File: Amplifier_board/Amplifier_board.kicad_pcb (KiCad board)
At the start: 2 copper layers, 100 x 100 mm, 167 parts, among them J1 Screw Terminal, J10 Conn_01x03_Pin, J11 Conn_01x03_Pin, J12 Conn_01x03_Pin, J13 Conn_01x03_Pin, J14 Conn_01x03_Pin, J15 Conn_01x03_Pin, J2 Screw Terminal, J3 Screw Terminal, J4 Screw Terminal, J5 Screw Terminal, J6 Screw Terminal, J7 A-DF_09_A_KG-T4S, J8 Conn_01x03_Pin, J9 Conn_01x03_Pin, U1 TPA3111D1PWPR, U2 TPA3111D1PWPR, U3 TPA3111D1PWPR, U4 TPA3111D1PWPR

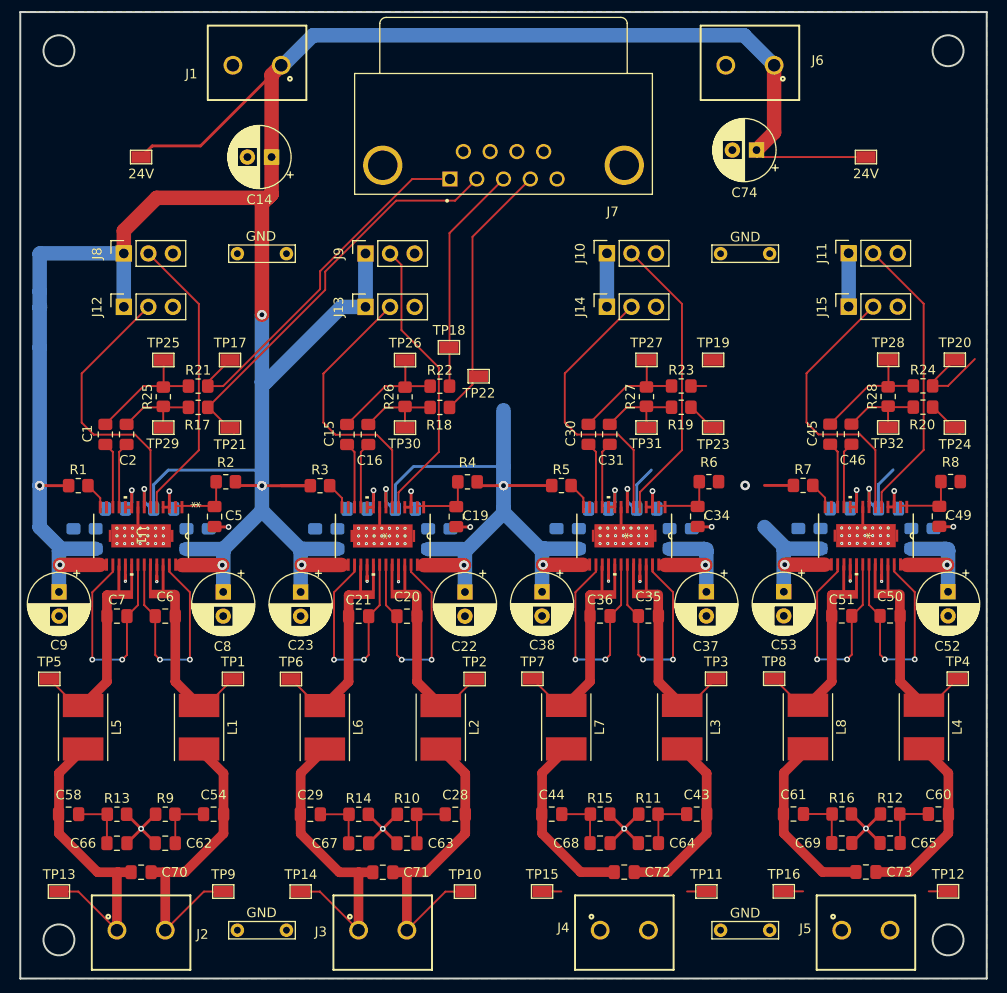
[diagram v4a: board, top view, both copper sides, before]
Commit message: Added test points, almost finished layout for amp board
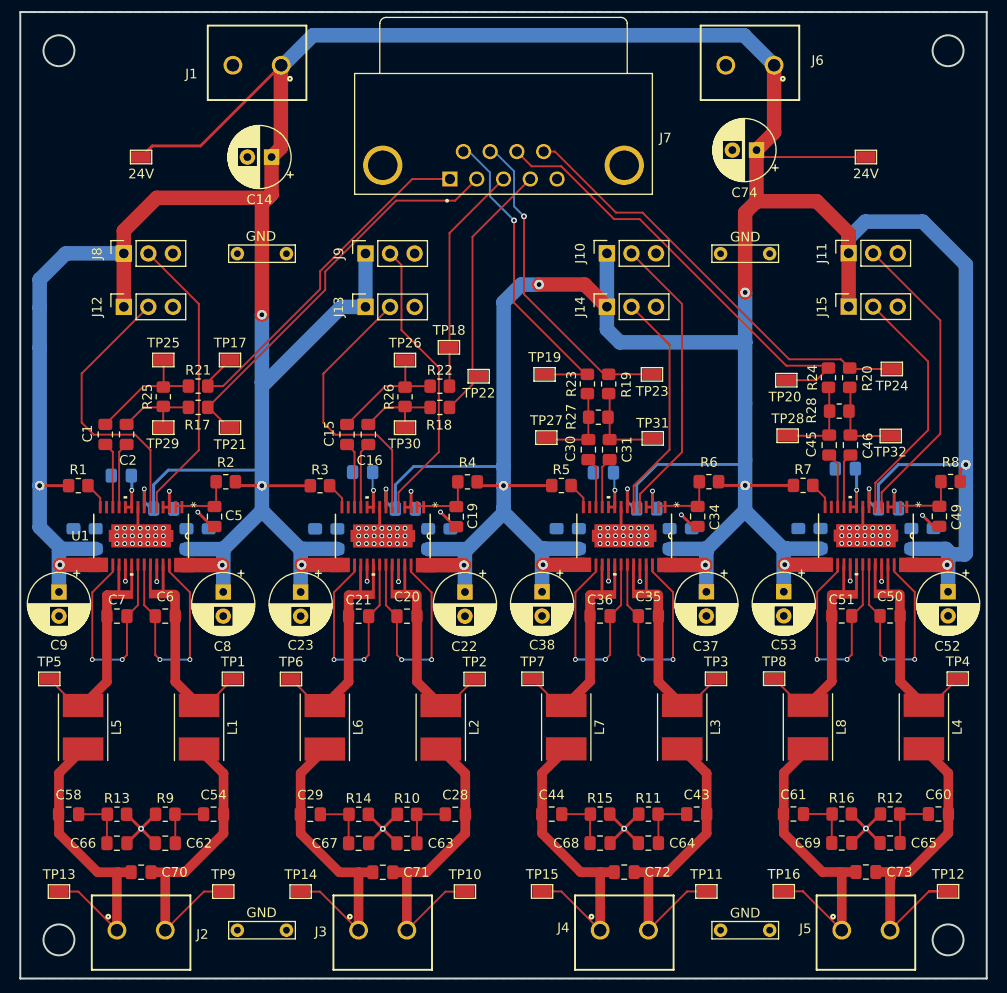
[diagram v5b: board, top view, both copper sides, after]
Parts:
- moved TP20 17.6 mm to (153.8, 77.6)
- moved TP19 17.5 mm to (128.8, 77.0)
- moved TP27 13.1 mm to (128.9, 83.5)
- moved TP28 13.0 mm to (153.9, 83.3)
- moved R24 9.82 mm to (158.1, 77.3), turned to 90 degrees
- moved R23 9.71 mm to (133.2, 78.0), turned to 90 degrees
- moved TP24 8.89 mm to (164.7, 76.4)
- moved TP23 8.39 mm to (139.9, 77.0)
- moved R20 8.17 mm to (160.3, 77.3), turned to 90 degrees
- moved R19 7.89 mm to (135.4, 78.0), turned to 90 degrees
- moved R27 5.42 mm to (134.3, 81.4), turned to 180 degrees
- moved R28 5.28 mm to (159.2, 80.8), turned to 180 degrees
- moved C48 4.17 mm to (159.9, 86.7)
- moved C18 3.84 mm to (109.9, 87.1)
- moved C33 3.77 mm to (134.8, 87.2)
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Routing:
- net +24V: track 455.1 -> 622.9 mm, vias 17 -> 20
- net /In4N: track 3.87 -> 45.3 mm
- net /In4P: track 9.74 -> 46.4 mm
- net /In3P: track 2.56 -> 33.8 mm, vias 0 -> 1
- net /In3N: track 3.87 -> 33.2 mm, vias 0 -> 1
- net /amp4/OutN: track 20.9 -> 34.7 mm
- net /amp4/OutP: track 20.9 -> 32.7 mm
- net /amp3/OutP: track 20.9 -> 32.6 mm
- net /amp3/OutN: track 20.9 -> 32.6 mm
- net /amp3/Gain1: track 29.0 -> 23.9 mm
- net Net-(C30-Pad1): track 13.2 -> 9.23 mm
- net Net-(C45-Pad1): track 13.2 -> 9.30 mm
- net /amp4/Gain1: track 29.0 -> 25.3 mm
- net Net-(U3-INN): track 6.81 -> 5.23 mm
- net Net-(U3-INP): track 6.81 -> 5.23 mm
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
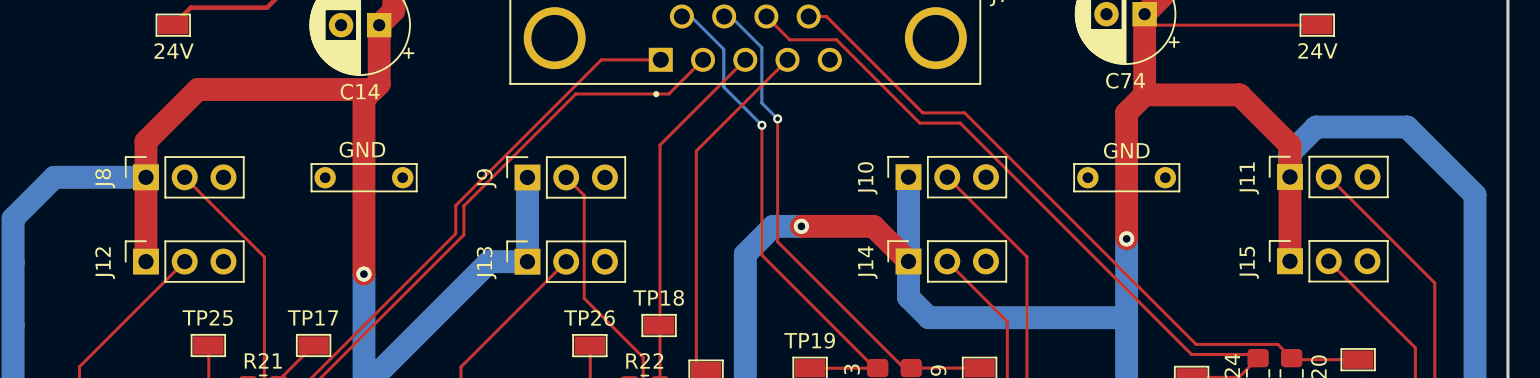
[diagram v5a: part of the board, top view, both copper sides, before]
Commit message: Updated silkscreen on amp board
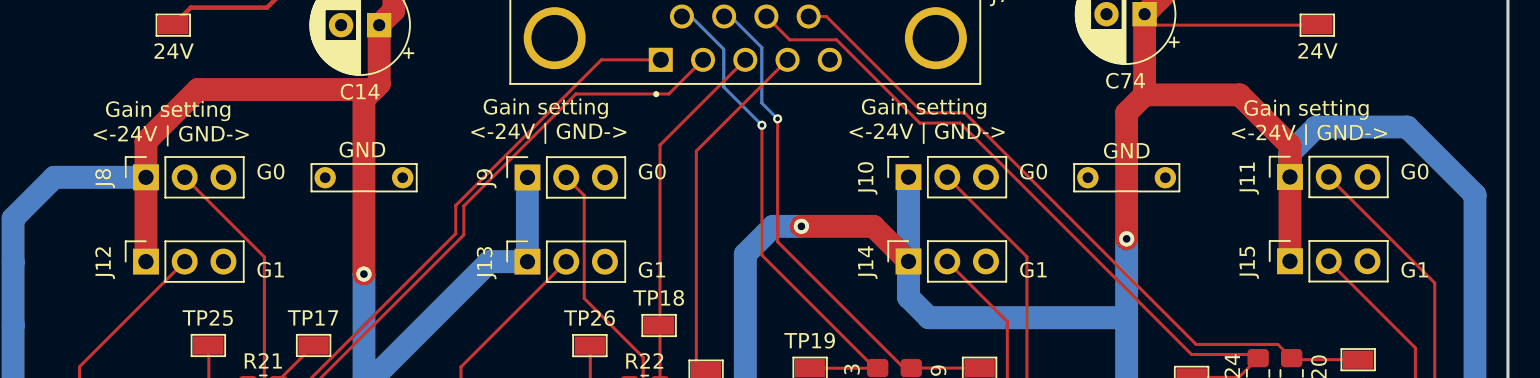
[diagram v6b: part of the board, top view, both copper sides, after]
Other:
- board text added: "G0 G1"
- board text added: "Gain setting <-24V | GND->"

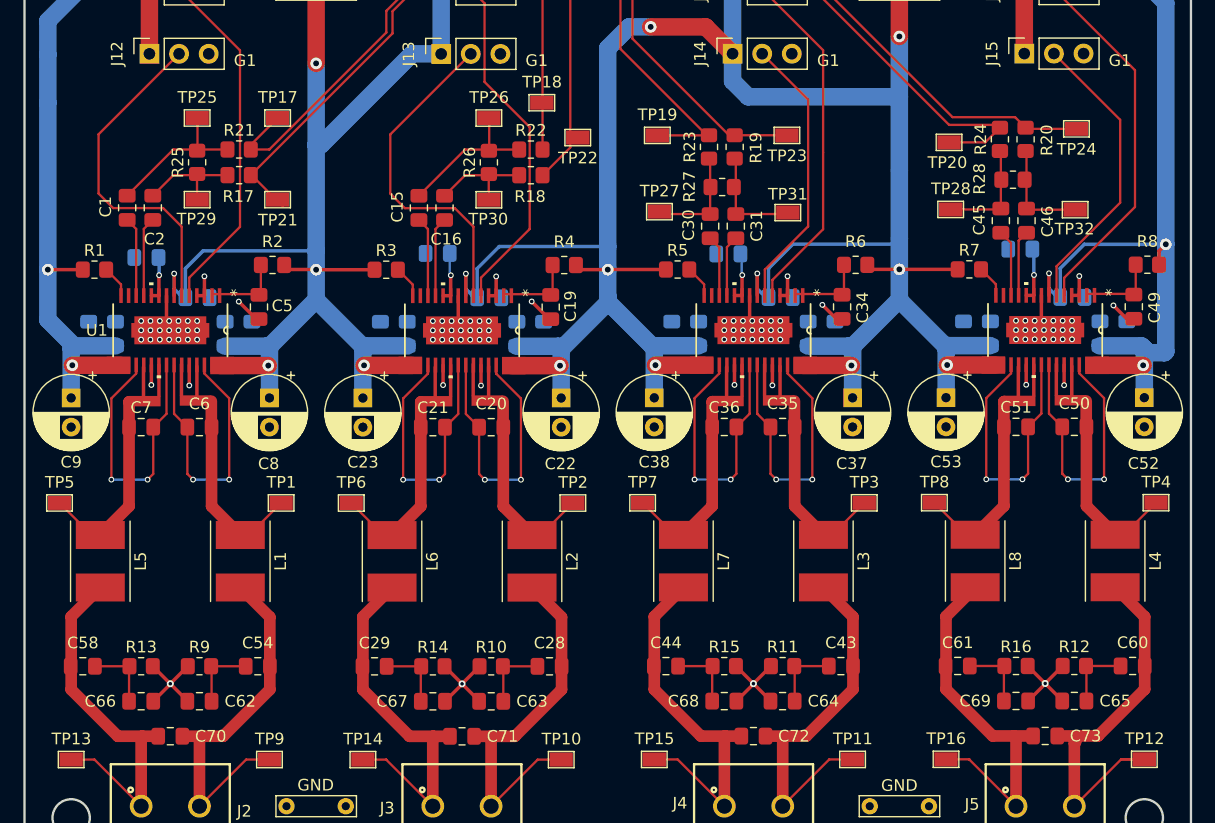
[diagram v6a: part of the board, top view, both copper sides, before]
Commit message: Added new MCU board footprint and symbol
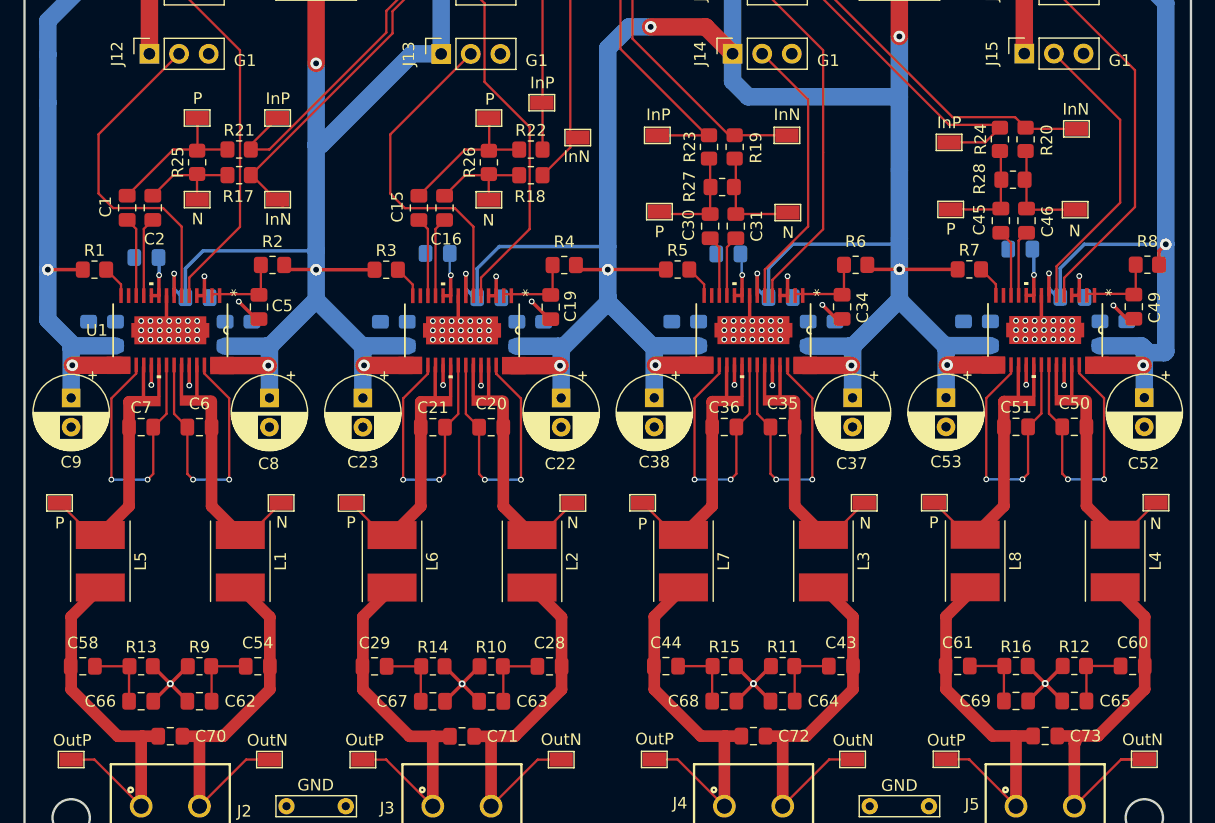
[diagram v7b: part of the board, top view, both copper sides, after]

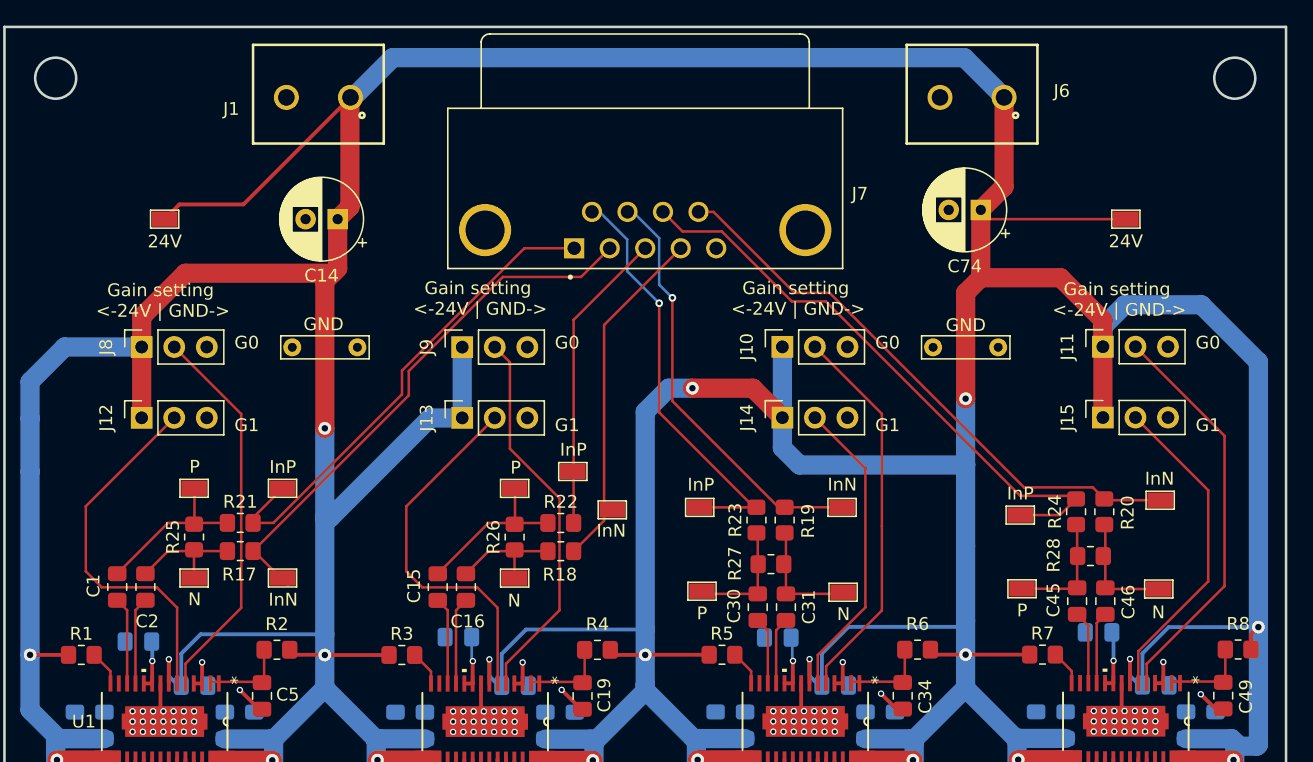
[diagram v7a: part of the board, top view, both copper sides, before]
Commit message: Schematic almost done on DAC board
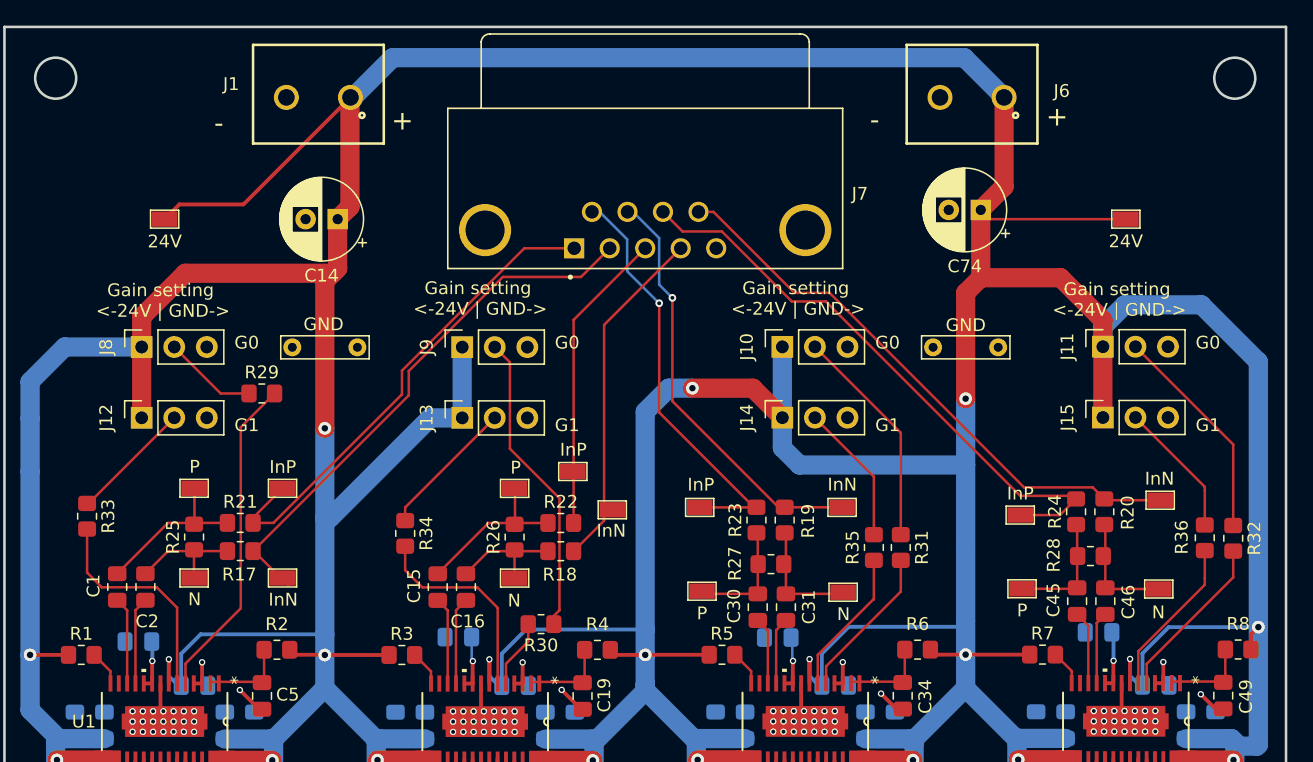
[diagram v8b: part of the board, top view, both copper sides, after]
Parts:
- added R29: 100k, Resistor_SMD:R_0805_2012Metric_Pad1.20x1.40mm_HandSolder, F.Cu at (94.6, 68.1)
- added R30: 100k, Resistor_SMD:R_0805_2012Metric_Pad1.20x1.40mm_HandSolder, F.Cu at (116.4, 86.1)
- added R31: 100k, Resistor_SMD:R_0805_2012Metric_Pad1.20x1.40mm_HandSolder, F.Cu at (144.4, 80.1)
- added R32: 100k, Resistor_SMD:R_0805_2012Metric_Pad1.20x1.40mm_HandSolder, F.Cu at (170.4, 79.4)
- added R33: 100k, Resistor_SMD:R_0805_2012Metric_Pad1.20x1.40mm_HandSolder, F.Cu at (81.0, 77.7)
- added R34: 100k, Resistor_SMD:R_0805_2012Metric_Pad1.20x1.40mm_HandSolder, F.Cu at (105.8, 79.0)
- added R35: 100k, Resistor_SMD:R_0805_2012Metric_Pad1.20x1.40mm_HandSolder, F.Cu at (142.3, 80.1)
- added R36: 100k, Resistor_SMD:R_0805_2012Metric_Pad1.20x1.40mm_HandSolder, F.Cu at (168.2, 79.4)
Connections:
- J10 pad 2: /amp3/Gain0 -> Net-(J10-Pin_2)
- J11 pad 2: /amp4/Gain0 -> Net-(J11-Pin_2)
- J12 pad 2: /amp1/Gain1 -> Net-(J12-Pin_2)
- J13 pad 2: /amp2/Gain1 -> Net-(J13-Pin_2)
- J14 pad 2: /amp3/Gain1 -> Net-(J14-Pin_2)
- J15 pad 2: /amp4/Gain1 -> Net-(J15-Pin_2)
- J8 pad 2: /amp1/Gain0 -> Net-(J8-Pin_2)
- J9 pad 2: /amp2/Gain0 -> Net-(J9-Pin_2)
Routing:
- net /amp2/Gain0: track 30.1 -> 5.35 mm
- net Net-(J9-Pin_2): track 0.00 -> 23.9 mm
- net /amp4/Gain0: track 31.6 -> 13.1 mm
- net /amp3/Gain0: track 30.2 -> 12.0 mm
- net Net-(J10-Pin_2): track 0.00 -> 17.4 mm
- net Net-(J11-Pin_2): track 0.00 -> 17.1 mm
- net /amp4/Gain1: track 25.3 -> 12.5 mm
- net /amp2/Gain1: track 29.0 -> 16.2 mm
- net /amp3/Gain1: track 23.9 -> 11.4 mm
- net /amp1/Gain1: track 29.0 -> 17.5 mm
- net Net-(J14-Pin_2): track 0.00 -> 11.0 mm
- net Net-(J13-Pin_2): track 0.00 -> 10.9 mm
- net Net-(J15-Pin_2): track 0.00 -> 10.6 mm
- net Net-(J12-Pin_2): track 0.00 -> 9.57 mm
- net Net-(J8-Pin_2): track 0.00 -> 7.33 mm
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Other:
- board text added: "+"
- board text added: "-"
